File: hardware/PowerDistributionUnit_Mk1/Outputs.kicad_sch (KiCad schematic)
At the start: 23 parts, among them U25 NL17SZS11DFT2G-Q

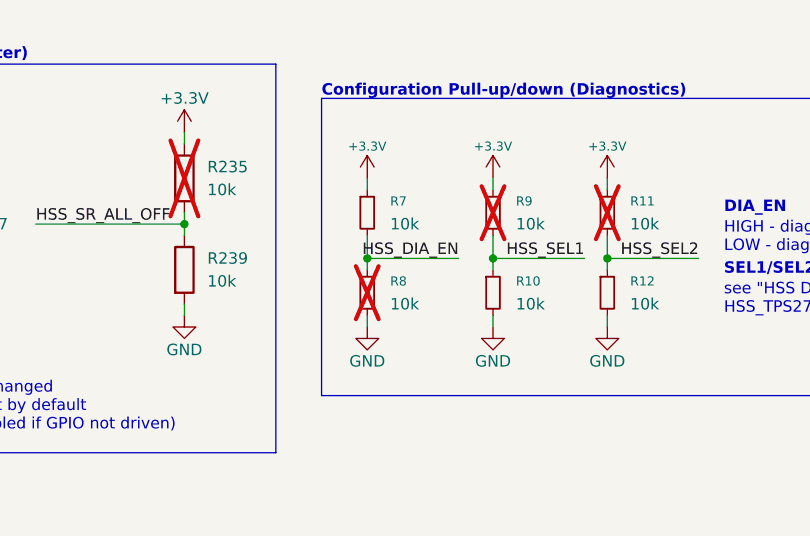
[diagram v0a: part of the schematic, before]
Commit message: change DNP to disable HSS diagnostics by default (primarily use external current sensor)
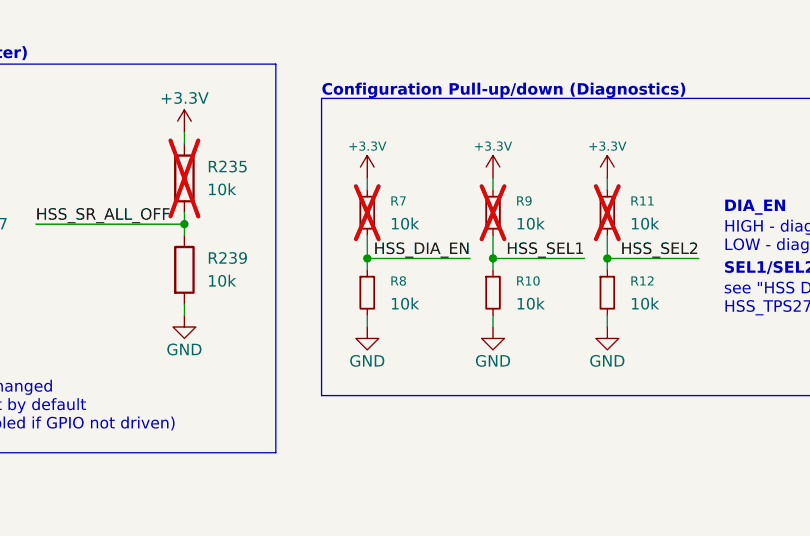
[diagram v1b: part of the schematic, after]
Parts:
- R7: now not fitted
- R8: now fitted
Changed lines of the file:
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@@
 	(wire
 		(pts
-			(xy 185.42 50.8) (xy 195.58 50.8)
+			(xy 185.42 50.8) (xy 196.85 50.8)
 		)
 		(stroke
@@
 	)
 	(label "HSS_DIA_EN"
-		(at 195.58 50.8 180)
+		(at 196.85 50.8 180)
 		(effects
 			(font
@@
 		(in_bom yes)
 		(on_board yes)
-		(dnp yes)
+		(dnp no)
 		(fields_autoplaced yes)
 		(property "Reference" "R8"
@@
 		(in_bom yes)
 		(on_board yes)
-		(dnp no)
+		(dnp yes)
 		(fields_autoplaced yes)
 		(property "Reference" "R7"
